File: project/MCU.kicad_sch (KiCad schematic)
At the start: 44 parts, among them IC301 ESDALC6V1W5, IC302 FAN5622SX, IC303 MX25U51245GZ4I00, IC304 TS3USB221A, IC305 NTS0104GU12, IC306 DRV2603RUNT, IC307 RV-8263-C8, M301 NORA-B106, M302 Vibrator DC Motor, Q301 BC817W, Q302 PMZ550UNEYL, Q303 PMZ550UNEYL, X301 DOCK, X302 GC9A01A_CST816S, X303 M+, X304 M-

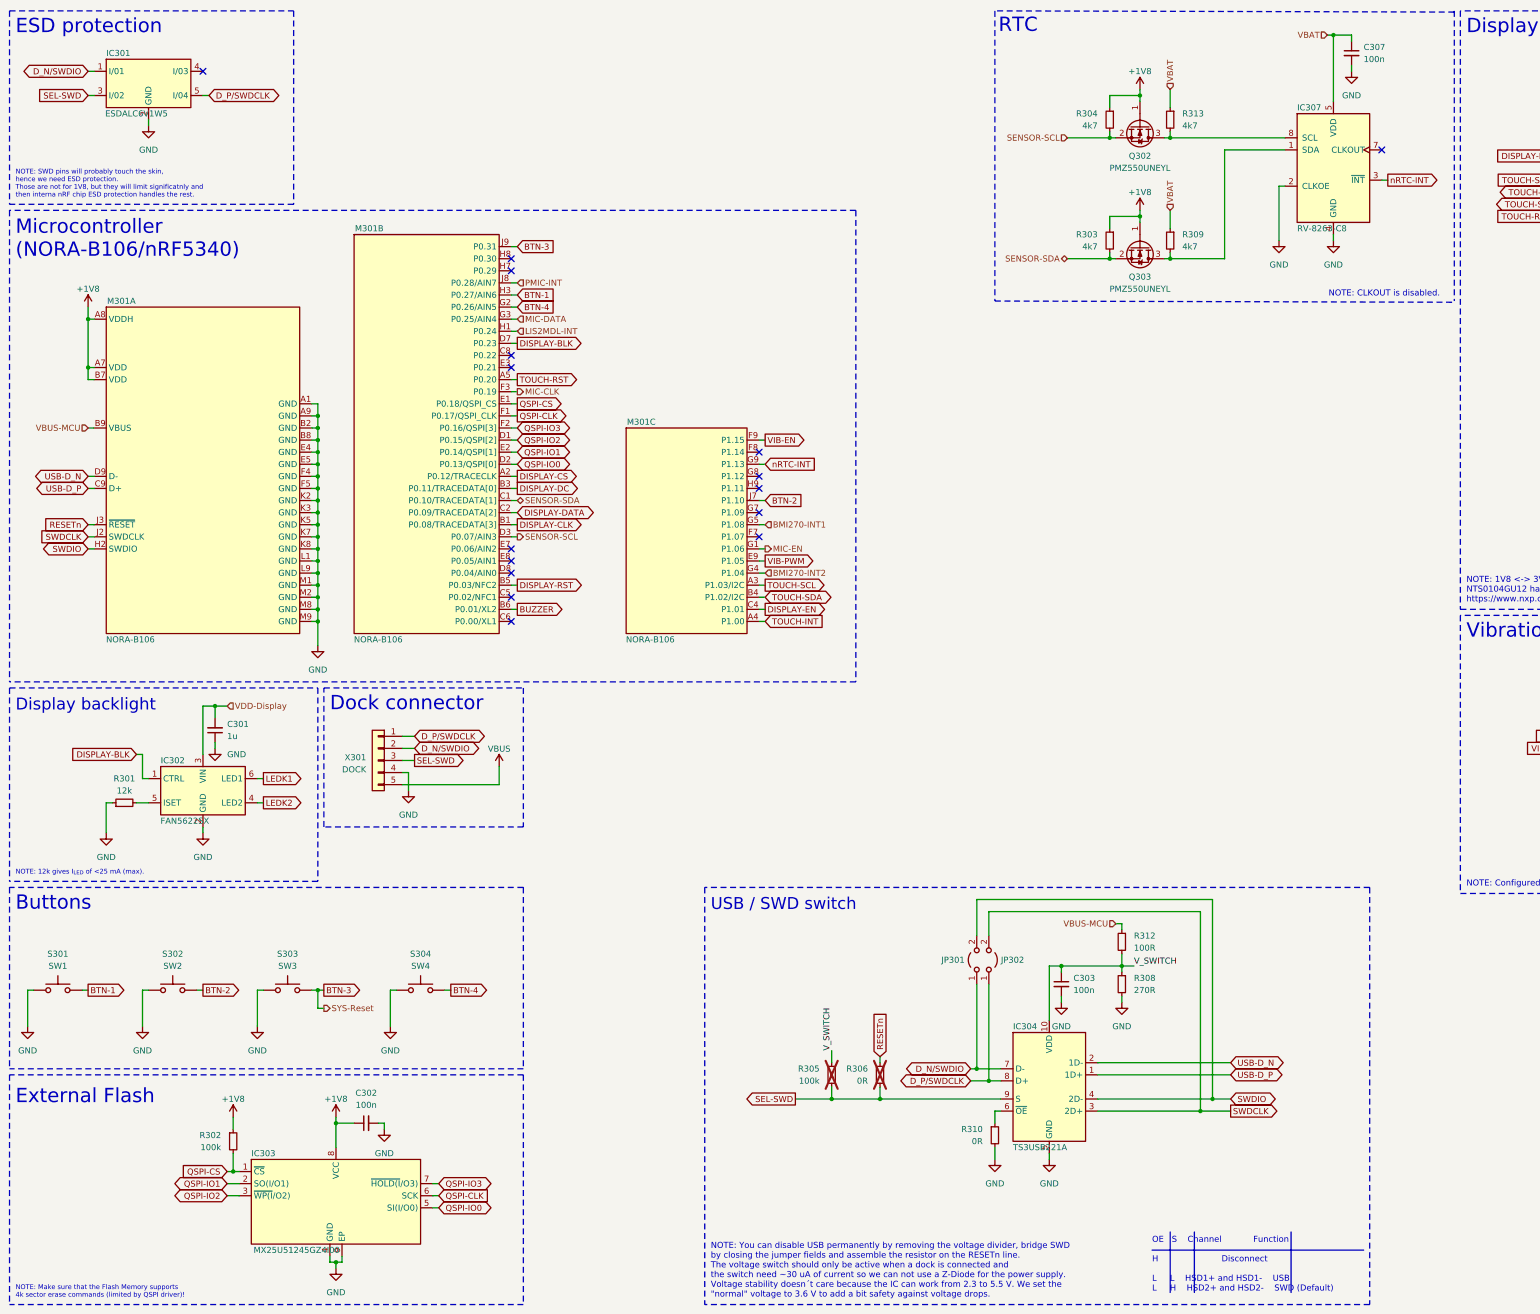
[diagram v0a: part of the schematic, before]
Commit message: PCB: Remove BME688 and USB switch
- Implement #106
- Remove USB switch and the required components

Signed-off-by: Daniel Kampert <danielkampert@kampis-elektroecke.de>
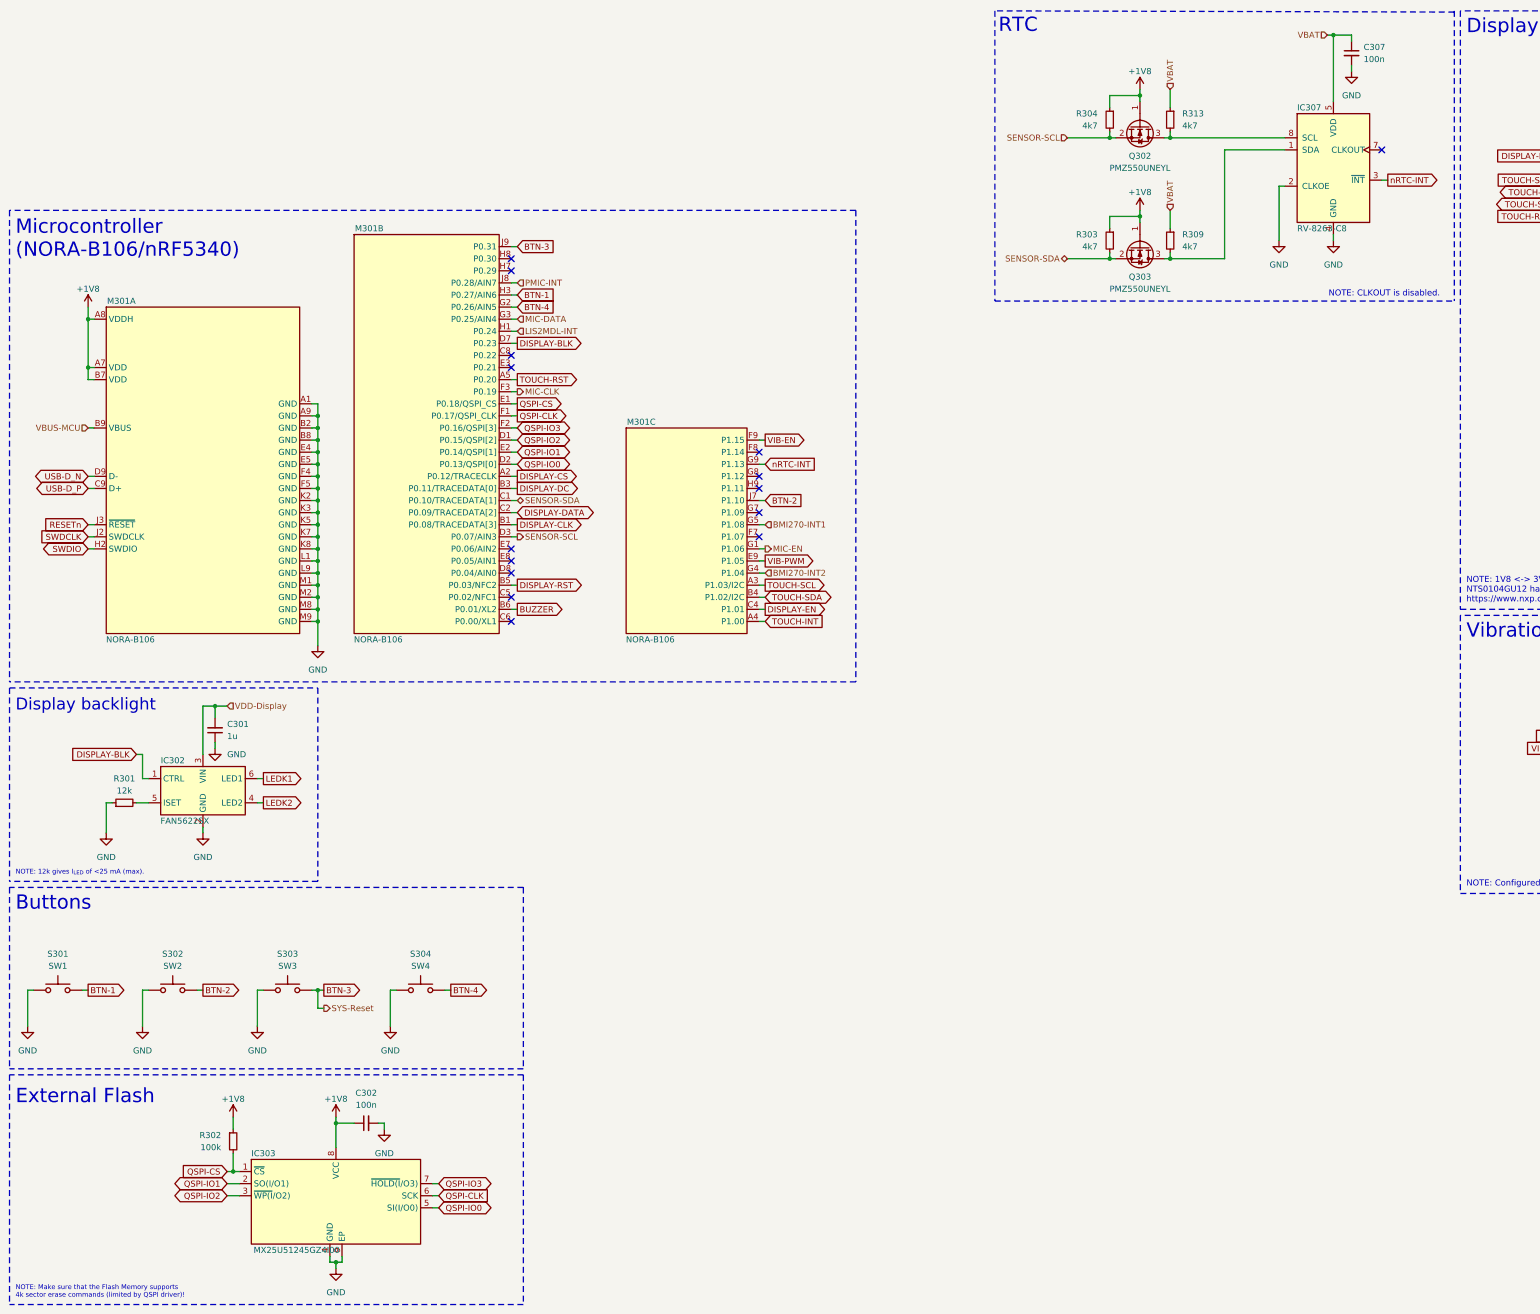
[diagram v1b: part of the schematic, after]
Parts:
- removed C303: 100n, Capacitor_SMD:C_0603_1608Metric, symbol Device:C_Small
- removed IC301: ESDALC6V1W5, Package_TO_SOT_SMD:SOT-665, symbol ST:ESDALC6V1P5
- removed IC304: TS3USB221A, Package_QFN:UQFN-10_1.55x2.05mm_P0.5mm, symbol TexasInstruments_Kampi:TS3USB221A
- removed JP301, JP302: ~, Jumper:SolderJumper-2_P1.3mm_Open_RoundedPad1.0x1.5mm, symbol Jumper:Jumper_2_Open
- removed R305: 100k, Resistor_SMD:R_0603_1608Metric, symbol Device:R_Small
- removed R306, R310: 0R, Resistor_SMD:R_0402_1005Metric, symbol Device:R_Small
- removed R308: 270R, Resistor_SMD:R_0603_1608Metric, symbol Device:R_Small
- removed R312: 100R, Resistor_SMD:R_0603_1608Metric, symbol Device:R_Small
- removed X301: DOCK, Pomagtor:RD90_LZH0230529-004_DJ-5PIN_PH2_54, symbol Connector_Generic:Conn_01x05
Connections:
- no-connect marks 17 -> 16
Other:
- note removed: "Dock connector"
- note removed: "ESD protection"
- note removed: "NOTE: SWD pins will probably touch the skin, hence we need ESD protection. Those are not for 1V8, but they will limit significatnly and then interna nRF chip ESD protection handles the rest."
- note removed: "NOTE: You can disable USB permanently by removing the voltage divider, bridge SWD by closing the jumper fields and assemble the resistor on the RESETn line. The voltage switch should only be active when a dock is connected and the switch need ~30 uA of current so we can not use a Z-Diode for the power supply. Voltage stability doesn´t care because the IC can work from 2.3 to 5.5 V. We set the "no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"
- note removed: "OE S Channel Function H Disconnect L L HSD1+ and HSD1- USB L H HSD2+ and HSD2- SWD (Default)"
- note removed: "USB / SWD switch"
- title: ZSWatch v2 -> ZSWatch v3

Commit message: Project: Port to KiCad 9
- Port to KiCad 9.0.1

Closes #101

Signed-off-by: Daniel Kampert <danielkampert@kampis-elektroecke.de>
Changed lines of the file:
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@@
 (kicad_sch
-	(version 20231120)
+	(version 20250114)
 	(generator "eeschema")
-	(generator_version "8.0")
+	(generator_version "9.0")
 	(paper "A3")
 	(title_block
 		(title "ZSWatch v3")
 		(date "2025-05-05")
-		(rev "1")
+		(rev "0")
 		(company "github.com/jakkra/ZSWatch-HW")
 	)
+	(text "NOTE: CLKOUT is disabled."
+		(exclude_from_sim no)
+		(at 289.814 72.898 0)
+		(effects
+			(font
+				(size 1.27 1.27)
+			)
+			(justify left bottom)
+		)
+	)
+	(text "Buttons"
+		(exclude_from_sim no)
+		(at 13.97 201.93 0)
+		(effects
+			(font
+				(size 3 3)
+			)
+			(justify left bottom)
+		)
+	)
+	(text "NOTE: 12k gives I_{LED} of <25 mA (max)."
+		(exclude_from_sim no)
+		(at 13.97 194.31 0)
+		(effects
+			(font
+				(size 1 1)
+			)
+			(justify left bottom)
+		)
+	)
+	(text "Vibration motor"
+		(exclude_from_sim no)
+		(at 318.77 144.78 0)
+		(effects
+			(font
+				(size 3 3)
+			)
+			(justify left bottom)
+		)
+	)
+	(text "Buzzer"
+		(exclude_from_sim no)
+		(at 359.41 212.09 0)
+		(effects
+			(font
+				(size 3 3)
+			)
+			(justify left bottom)
+		)
+	)
+	(text "NOTE: Make sure that the Flash Memory supports\n4k sector erase commands (limited by QSPI driver)!"
+		(exclude_from_sim no)
+		(at 13.97 283.21 0)
+		(effects
+			(font
+				(size 1 1)
+			)
+			(justify left bottom)
+		)
+	)
+	(text "RTC"
+		(exclude_from_sim no)
+		(at 220.472 17.526 0)
+		(effects
+			(font
+				(size 3 3)
+			)
+			(justify left bottom)
+		)
+	)
+	(text "Display"
+		(exclude_from_sim no)
+		(at 318.77 17.78 0)
+		(effects
+			(font
+				(size 3 3)
+			)
+			(justify left bottom)
+		)
+	)
+	(text "NOTE: 1V8 <-> 3V3 level shifter\nNTS0104GU12 has internal pullups. Works for I2C.\nhttps://www.nxp.com/docs/en/data-sheet/NTS0104.pdf"
+		(exclude_from_sim no)
+		(at 318.77 137.16 0)
+		(effects
+			(font
+				(size 1.27 1.27)
+			)
+			(justify left bottom)
+		)
+	)
+	(text "Microcontroller\n(NORA-B106/nRF5340)"
+		(exclude_from_sim no)
+		(at 13.97 64.77 0)
+		(effects
+			(font
+				(size 3 3)
+			)
+			(justify left bottom)
+		)
+	)
+	(text "Display backlight"
+		(exclude_from_sim no)
+		(at 13.97 160.02 0)
+		(effects
+			(font
+				(size 2.5 2.5)
+			)
+			(justify left bottom)
+		)
+	)
+	(text "NOTE: Configured for ERM mode."
+		(exclude_from_sim no)
+		(at 318.77 196.85 0)
+		(effects
+			(font
+				(size 1.27 1.27)
+			)
+			(justify left bottom)
+		)
+	)
+	(text "External Flash"
+		(exclude_from_sim no)
+		(at 13.97 242.57 0)
+		(effects
+			(font
+				(size 3 3)
+			)
+			(justify left bottom)
+		)
+	)
 	(junction
 		(at 77.47 123.19)
@@
 		)
 	)
-	(text "NOTE: CLKOUT is disabled."
-		(exclude_from_sim no)
-		(at 289.814 72.898 0)
-		(effects
-			(font
-				(size 1.27 1.27)
-			)
-			(justify left bottom)
-		)
-	)
-	(text "Buttons"
-		(exclude_from_sim no)
-		(at 13.97 201.93 0)
-		(effects
-			(font
-				(size 3 3)
-			)
-			(justify left bottom)
-		)
-	)
-	(text "NOTE: 12k gives I_{LED} of <25 mA (max)."
-		(exclude_from_sim no)
-		(at 13.97 194.31 0)
-		(effects
-			(font
-				(size 1 1)
-			)
-			(justify left bottom)
-		)
-	)
-	(text "Vibration motor"
-		(exclude_from_sim no)
-		(at 318.77 144.78 0)
-		(effects
-			(font
-				(size 3 3)
-			)
-			(justify left bottom)
-		)
-	)
-	(text "Buzzer"
-		(exclude_from_sim no)
-		(at 359.41 212.09 0)
-		(effects
-			(font
-				(size 3 3)
-			)
-			(justify left bottom)
-		)
-	)
-	(text "NOTE: Make sure that the Flash Memory supports\n4k sector erase commands (limited by QSPI driver)!"
-		(exclude_from_sim no)
-		(at 13.97 283.21 0)
-		(effects
-			(font
-				(size 1 1)
-			)
-			(justify left bottom)
-		)
-	)
-	(text "RTC"
-		(exclude_from_sim no)
-		(at 220.472 17.526 0)
-		(effects
-			(font
-				(size 3 3)
-			)
-			(justify left bottom)
-		)
-	)
-	(text "Display"
-		(exclude_from_sim no)
-		(at 318.77 17.78 0)
-		(effects
-			(font
-				(size 3 3)
-			)
-			(justify left bottom)
-		)
-	)
-	(text "NOTE: 1V8 <-> 3V3 level shifter\nNTS0104GU12 has internal pullups. Works for I2C.\nhttps://www.nxp.com/docs/en/data-sheet/NTS0104.pdf"
-		(exclude_from_sim no)
-		(at 318.77 137.16 0)
-		(effects
-			(font
-				(size 1.27 1.27)
-			)
-			(justify left bottom)
-		)
-	)
-	(text "Microcontroller\n(NORA-B106/nRF5340)"
-		(exclude_from_sim no)
-		(at 13.97 64.77 0)
-		(effects
-			(font
-				(size 3 3)
-			)
-			(justify left bottom)
-		)
-	)
-	(text "Display backlight"
-		(exclude_from_sim no)
-		(at 13.97 160.02 0)
-		(effects
-			(font
-				(size 2.5 2.5)
-			)
-			(justify left bottom)
-		)
-	)
-	(text "NOTE: Configured for ERM mode."
-		(exclude_from_sim no)
-		(at 318.77 196.85 0)
-		(effects
-			(font
-				(size 1.27 1.27)
-			)
-			(justify left bottom)
-		)
-	)
-	(text "External Flash"
-		(exclude_from_sim no)
-		(at 13.97 242.57 0)
-		(effects
-			(font
-				(size 3 3)
-			)
-			(justify left bottom)
-		)
-	)
 	(global_label "QSPI-CLK"
 		(shape output)
@@
 		(shape input)
 		(at 234.95 39.37 180)
-		(fields_autoplaced yes)
 		(effects
 			(font
@@
 		(shape bidirectional)
 		(at 234.95 64.77 180)
-		(fields_autoplaced yes)
 		(effects
 			(font
@@
 		(shape input)
 		(at 119.38 69.85 0)
-		(fields_autoplaced yes)
 		(effects
 			(font
@@
 		(shape input)
 		(at 374.65 73.66 0)
-		(fields_autoplaced yes)
 		(effects
 			(font
@@
 		(shape input)
 		(at 58.42 158.75 0)
-		(fields_autoplaced yes)
 		(effects
 			(font
@@
 		(shape input)
 		(at 256.54 54.61 90)
-		(fields_autoplaced yes)
 		(effects
 			(font
@@
 		(shape input)
 		(at 119.38 77.47 0)
-		(fields_autoplaced yes)
 		(effects
 			(font
@@
 		(shape input)
 		(at 384.81 110.49 0)
-		(fields_autoplaced yes)
 		(effects
 			(font
@@
 		(shape output)
 		(at 171.45 125.73 0)
-		(fields_autoplaced yes)
 		(effects
 			(font
@@
 		(shape input)
 		(at 29.21 100.33 180)
-		(fields_autoplaced yes)
 		(effects
 			(font
@@
 		(shape input)
 		(at 355.6 17.78 0)
-		(fields_autoplaced yes)
 		(effects
 			(font
@@
 		(shape input)
 		(at 256.54 29.21 90)
-		(fields_autoplaced yes)
 		(effects
 			(font
@@
 		(shape input)
 		(at 289.56 17.78 180)
-		(fields_autoplaced yes)
 		(effects
 			(font
@@
 		(shape input)
 		(at 171.45 130.81 0)
-		(fields_autoplaced yes)
 		(effects
 			(font
@@
 		(shape output)
 		(at 119.38 123.19 0)
-		(fields_autoplaced yes)
 		(effects
 			(font
@@
 		(shape input)
 		(at 171.45 120.65 0)
-		(fields_autoplaced yes)
 		(effects
 			(font
@@
 		(shape output)
 		(at 119.38 92.71 0)
-		(fields_autoplaced yes)
 		(effects
 			(font
@@
 		(shape bidirectional)
 		(at 119.38 115.57 0)
-		(fields_autoplaced yes)
 		(effects
 			(font
@@
 		(shape input)
 		(at 356.87 148.59 180)
-		(fields_autoplaced yes)
 		(effects
 			(font
@@
 		(shape input)
 		(at 119.38 80.01 0)
-		(fields_autoplaced yes)
 		(effects
 			(font
@@
 		(shape output)
 		(at 78.74 222.25 0)
-		(fields_autoplaced yes)
 		(effects
 			(font
